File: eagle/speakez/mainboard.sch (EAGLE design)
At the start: 27 parts, among them U1 +12v

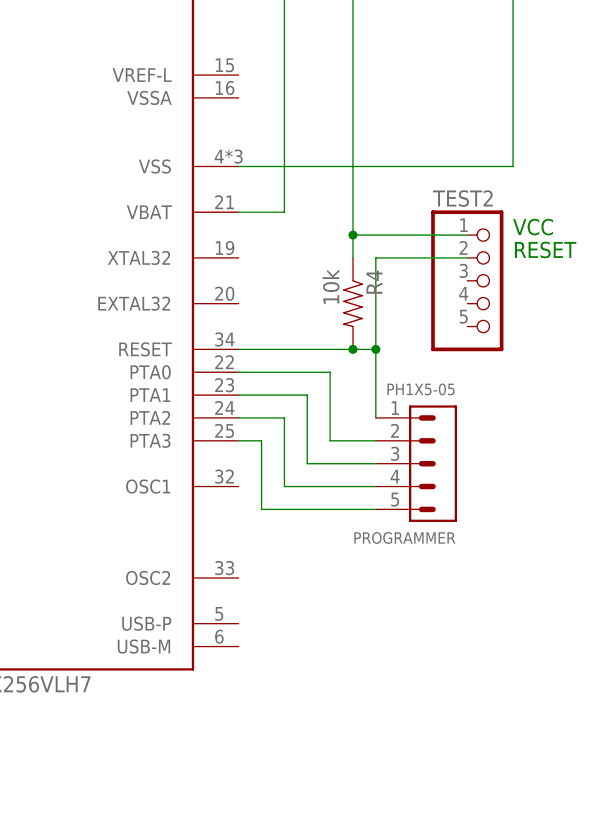
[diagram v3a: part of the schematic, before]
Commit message: Added correct header for programmer
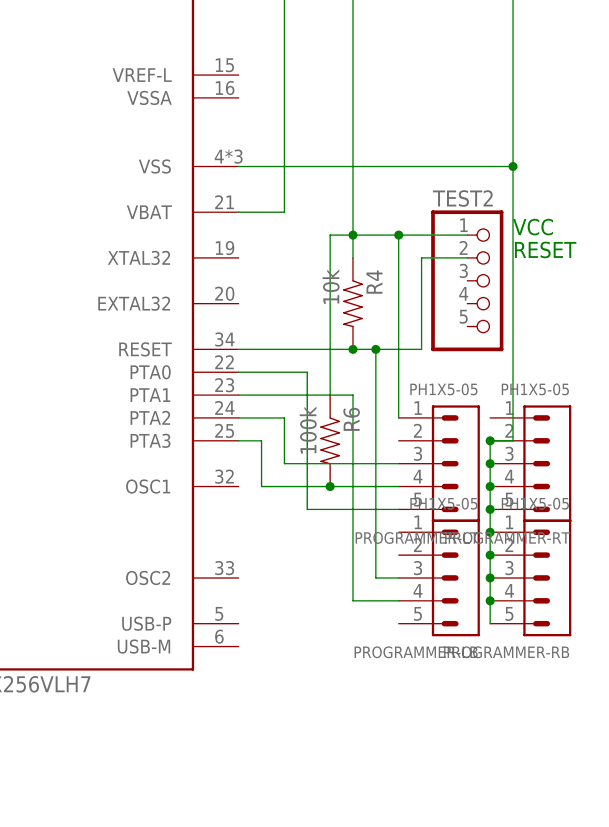
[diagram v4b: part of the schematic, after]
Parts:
- removed PROGRAMMER: PH1X5-05, pel_hdr:PH1X5-05
- added PROGRAMMER-LB, PROGRAMMER-LT, PROGRAMMER-RB, PROGRAMMER-RT: PH1X5-05, pel_hdr:PH1X5-05
- added R6: 100k, SparkFun-Passives:RESISTOR0805-RES
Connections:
- removed net N$22: PROGRAMMER.3, U$1.PTA1
- new net N$29: BATTERY.2, C6.2, C7.2, C8.2, PROGRAMMER-RB.1, PROGRAMMER-RB.2, PROGRAMMER-RB.3, PROGRAMMER-RB.4, PROGRAMMER-RB.5, PROGRAMMER-RT.2, PROGRAMMER-RT.3, PROGRAMMER-RT.4, PROGRAMMER-RT.5, SERIAL.4, U$1.VSS, U1.GND
- net N$14: now also PROGRAMMER-LT.5, U$1.PTA0; no longer BATTERY.2, C6.2, C7.2, C8.2, SERIAL.4, U$1.VSS, U1.GND
- net N$16: now also PROGRAMMER-LT.1, R6.1
- net N$20: now also PROGRAMMER-LB.3; no longer PROGRAMMER.1
- net N$21: now also PROGRAMMER-LB.4, U$1.PTA1; no longer PROGRAMMER.2, U$1.PTA0
- net N$23: now also PROGRAMMER-LT.3; no longer PROGRAMMER.4
- net N$24: now also PROGRAMMER-LT.4, R6.2; no longer PROGRAMMER.5

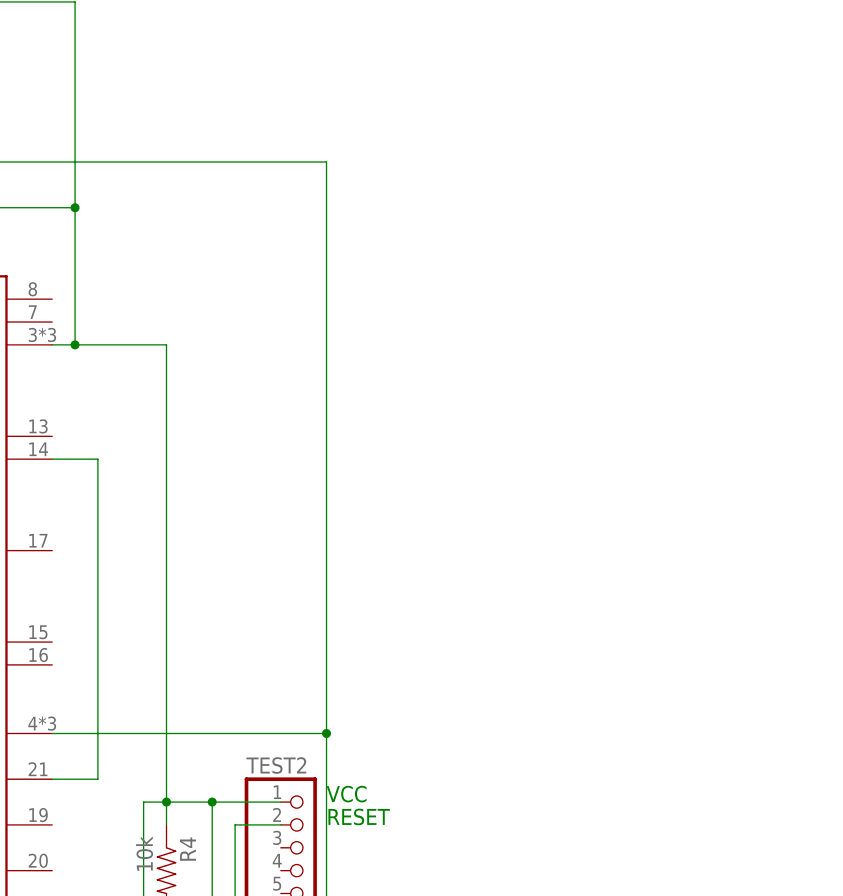
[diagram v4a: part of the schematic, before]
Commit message: added decoupling caps
to microcontroller VCC pin
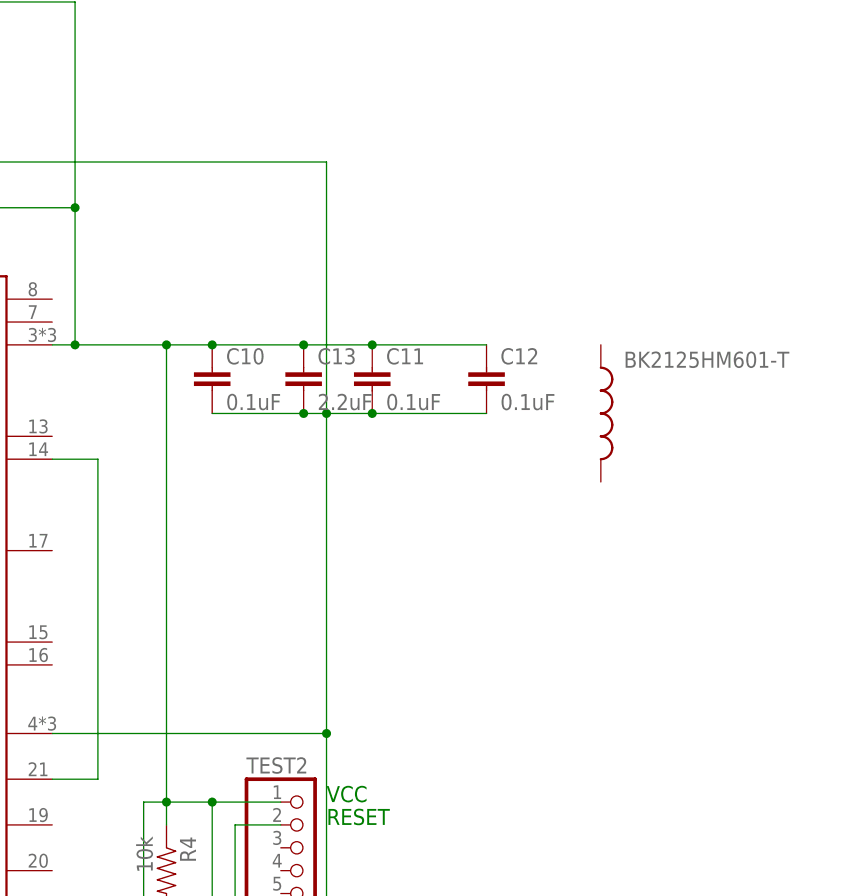
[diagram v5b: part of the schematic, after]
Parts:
- added BK2125HM601-T: (no value), SparkFun-Passives:INDUCTOR0805
- added C10, C11, C12: 0.1uF, SparkFun-Capacitors:CAP0805
- added C13: 2.2uF, SparkFun-Capacitors:CAP0805
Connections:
- removed net N$29: BATTERY.2, C6.2, C7.2, C8.2, PROGRAMMER-RB.1, PROGRAMMER-RB.2, PROGRAMMER-RB.3, PROGRAMMER-RB.4, PROGRAMMER-RB.5, PROGRAMMER-RT.2, PROGRAMMER-RT.3, PROGRAMMER-RT.4, PROGRAMMER-RT.5, SERIAL.4, U$1.VSS, U1.GND
- new net N$22: BATTERY.2, C10.2, C11.2, C12.2, C13.2, C6.2, C7.2, C8.2, PROGRAMMER-RB.1, PROGRAMMER-RB.2, PROGRAMMER-RB.3, PROGRAMMER-RB.4, PROGRAMMER-RB.5, PROGRAMMER-RT.2, PROGRAMMER-RT.3, PROGRAMMER-RT.4, PROGRAMMER-RT.5, SERIAL.4, U$1.VSS, U1.GND
- net N$16: now also C10.1, C11.1, C12.1, C13.1
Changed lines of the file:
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@@
 <part name="PROGRAMMER-RB" library="pel_hdr" deviceset="PH1X5" device="-05"/>
 <part name="R6" library="SparkFun-Passives" deviceset="RESISTOR" device="0805-RES" value="100k"/>
+<part name="C10" library="SparkFun-Capacitors" deviceset="CAP" device="0805" value="0.1uF"/>
+<part name="C11" library="SparkFun-Capacitors" deviceset="CAP" device="0805" value="0.1uF"/>
+<part name="C12" library="SparkFun-Capacitors" deviceset="CAP" device="0805" value="0.1uF"/>
+<part name="BK2125HM601-T" library="SparkFun-Passives" deviceset="INDUCTOR" device="0805"/>
+<part name="C13" library="SparkFun-Capacitors" deviceset="CAP" device="0805" value="2.2uF"/>
 </parts>
 <sheets>
@@
 <instance part="PROGRAMMER-RB" gate="G$1" x="210.82" y="-20.32" rot="R180"/>
 <instance part="R6" gate="G$1" x="185.42" y="-10.16" rot="R270"/>
+<instance part="C10" gate="G$1" x="193.04" y="58.42"/>
+<instance part="C11" gate="G$1" x="210.82" y="58.42"/>
+<instance part="C12" gate="G$1" x="223.52" y="58.42"/>
+<instance part="BK2125HM601-T" gate="G$1" x="236.22" y="55.88"/>
+<instance part="C13" gate="G$1" x="203.2" y="58.42"/>
 </instances>
 <busses>
@@
 <pinref part="R6" gate="G$1" pin="1"/>
 <wire x1="185.42" y1="12.7" x2="185.42" y2="-5.08" width="0.1524" layer="91"/>
+<wire x1="187.96" y1="63.5" x2="193.04" y2="63.5" width="0.1524" layer="91"/>
+<junction x="187.96" y="63.5"/>
+<pinref part="C10" gate="G$1" pin="1"/>
+<wire x1="193.04" y1="63.5" x2="203.2" y2="63.5" width="0.1524" layer="91"/>
+<junction x="193.04" y="63.5"/>
+<pinref part="C11" gate="G$1" pin="1"/>
+<wire x1="203.2" y1="63.5" x2="210.82" y2="63.5" width="0.1524" layer="91"/>
+<wire x1="210.82" y1="63.5" x2="223.52" y2="63.5" width="0.1524" layer="91"/>
+<junction x="210.82" y="63.5"/>
+<pinref part="C12" gate="G$1" pin="1"/>
+<pinref part="C13" gate="G$1" pin="1"/>
+<junction x="203.2" y="63.5"/>
 </segment>
 </net>
@@
 </segment>
 </net>
-<net name="N$29" class="0">
-<segment>
+<net name="N$14" class="0">
+<segment>
+<pinref part="U$1" gate="G$1" pin="PTA0"/>
+<wire x1="175.26" y1="-2.54" x2="182.88" y2="-2.54" width="0.1524" layer="91"/>
+<wire x1="182.88" y1="-2.54" x2="182.88" y2="-17.78" width="0.1524" layer="91"/>
+<pinref part="PROGRAMMER-LT" gate="G$1" pin="5"/>
+<wire x1="182.88" y1="-17.78" x2="193.04" y2="-17.78" width="0.1524" layer="91"/>
+</segment>
+</net>
+<net name="N$21" class="0">
+<segment>
+<pinref part="U$1" gate="G$1" pin="PTA1"/>
+<wire x1="175.26" y1="-5.08" x2="187.96" y2="-5.08" width="0.1524" layer="91"/>
+<wire x1="187.96" y1="-5.08" x2="187.96" y2="-27.94" width="0.1524" layer="91"/>
+<pinref part="PROGRAMMER-LB" gate="G$1" pin="4"/>
+<wire x1="187.96" y1="-27.94" x2="193.04" y2="-27.94" width="0.1524" layer="91"/>
+</segment>
+</net>
+<net name="N$22" class="0">
+<segment>
+<pinref part="C11" gate="G$1" pin="2"/>
+<pinref part="C12" gate="G$1" pin="2"/>
+<wire x1="210.82" y1="55.88" x2="223.52" y2="55.88" width="0.1524" layer="91"/>
 <pinref part="PROGRAMMER-RT" gate="G$1" pin="2"/>
 <pinref part="PROGRAMMER-RT" gate="G$1" pin="3"/>
@@
 <junction x="139.7" y="83.82"/>
 <wire x1="149.86" y1="83.82" x2="205.74" y2="83.82" width="0.1524" layer="91"/>
-<wire x1="205.74" y1="83.82" x2="205.74" y2="20.32" width="0.1524" layer="91"/>
+<wire x1="205.74" y1="83.82" x2="205.74" y2="55.88" width="0.1524" layer="91"/>
 <pinref part="U$1" gate="G$1" pin="VSS"/>
+<wire x1="205.74" y1="55.88" x2="205.74" y2="20.32" width="0.1524" layer="91"/>
 <wire x1="205.74" y1="20.32" x2="175.26" y2="20.32" width="0.1524" layer="91"/>
 <pinref part="C7" gate="G$1" pin="2"/>
@@
 <junction x="203.2" y="-10.16"/>
 <junction x="205.74" y="20.32"/>
-</segment>
-</net>
-<net name="N$14" class="0">
-<segment>
-<pinref part="U$1" gate="G$1" pin="PTA0"/>
-<wire x1="175.26" y1="-2.54" x2="182.88" y2="-2.54" width="0.1524" layer="91"/>
-<wire x1="182.88" y1="-2.54" x2="182.88" y2="-17.78" width="0.1524" layer="91"/>
-<pinref part="PROGRAMMER-LT" gate="G$1" pin="5"/>
-<wire x1="182.88" y1="-17.78" x2="193.04" y2="-17.78" width="0.1524" layer="91"/>
-</segment>
-</net>
-<net name="N$21" class="0">
-<segment>
-<pinref part="U$1" gate="G$1" pin="PTA1"/>
-<wire x1="175.26" y1="-5.08" x2="187.96" y2="-5.08" width="0.1524" layer="91"/>
-<wire x1="187.96" y1="-5.08" x2="187.96" y2="-27.94" width="0.1524" layer="91"/>
-<pinref part="PROGRAMMER-LB" gate="G$1" pin="4"/>
-<wire x1="187.96" y1="-27.94" x2="193.04" y2="-27.94" width="0.1524" layer="91"/>
-</segment>
-</net>
+<wire x1="210.82" y1="55.88" x2="205.74" y2="55.88" width="0.1524" layer="91"/>
+<junction x="210.82" y="55.88"/>
+<junction x="205.74" y="55.88"/>
+<pinref part="C10" gate="G$1" pin="2"/>
+<wire x1="193.04" y1="55.88" x2="203.2" y2="55.88" width="0.1524" layer="91"/>
+<pinref part="C13" gate="G$1" pin="2"/>
+<wire x1="203.2" y1="55.88" x2="205.74" y2="55.88" width="0.1524" layer="91"/>
+<junction x="203.2" y="55.88"/>
+</segment>
+</net>

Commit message: finished copying over Teensy schematic
Added a few more caps and ferrite beads to the microcontroller pins. I
didn't connect VREF-H directly to VBAT. Added test pins.
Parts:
- added BK2125HM601-T1: (no value), SparkFun-Passives:INDUCTOR0805
- added C14, C15, C16: 0.1uF, SparkFun-Capacitors:CAP0805
- added C17: 2.2uF, SparkFun-Capacitors:CAP0805
- added R7: 470, SparkFun-Passives:RESISTOR0805-RES
- TEST2: device pinhead:PINHD-1X5 -> pinhead:PINHD-1X7
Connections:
- removed net N$16: C10.1, C11.1, C12.1, C13.1, C4.2, C6.1, C8.1, PROGRAMMER-LT.1, R4.1, R6.1, SERIAL.3, TEST2.1, U$1.VCC, U1.OUT, VOICE.VDD
- new net N$29: BK2125HM601-T1.1, C15.2, C16.2, C17.2, TEST2.5, U$1.VREF-L, U$1.VSSA
- new net N$30: BK2125HM601-T.2, C17.1, R7.2, TEST2.3, U$1.VCCA
- new net N$31: C15.1, U$1.VREF_OUT
- net GND: now also BATTERY.2, BK2125HM601-T1.2, C10.2, C11.2, C12.2, C13.2, C14.2, C6.2, C7.2, C8.2, PROGRAMMER-RB.1, PROGRAMMER-RB.2, PROGRAMMER-RB.3, PROGRAMMER-RB.4, PROGRAMMER-RB.5, PROGRAMMER-RT.2, PROGRAMMER-RT.3, PROGRAMMER-RT.4, PROGRAMMER-RT.5, SERIAL.4, U$1.VSS, U1.GND
- net N$22: now also C16.1, R7.1, TEST2.4, U$1.VREF-H; no longer BATTERY.2, C10.2, C11.2, C12.2, C13.2, C6.2, C7.2, C8.2, PROGRAMMER-RB.1, PROGRAMMER-RB.2, PROGRAMMER-RB.3, PROGRAMMER-RB.4, PROGRAMMER-RB.5, PROGRAMMER-RT.2, PROGRAMMER-RT.3, PROGRAMMER-RT.4, PROGRAMMER-RT.5, SERIAL.4, U$1.VSS, U1.GND
- net N$3: now also BK2125HM601-T.1, C10.1, C11.1, C12.1, C13.1, C14.1, C4.2, C6.1, C8.1, PROGRAMMER-LT.1, R4.1, R6.1, SERIAL.3, TEST2.1, TEST2.6, TEST2.7, U$1.VCC, U1.OUT, VOICE.VDD; no longer U$1.VREF-H
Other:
- note added: "VBAT"
- note added: "VCCA"
- note added: "VREF-H"
- note added: "VREF-L/VSSA"
- note added: "VSS"
